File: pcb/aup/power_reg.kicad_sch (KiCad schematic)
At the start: 47 parts, among them Q2 AO3400A, Q3 AO3401A, U14 ISL80103IRAJZ-TK, U5 TPS563257DRLR, U6 ISL80103IRAJZ-TK, U8 TPS563257DRLR, U9 TPS563257DRLR

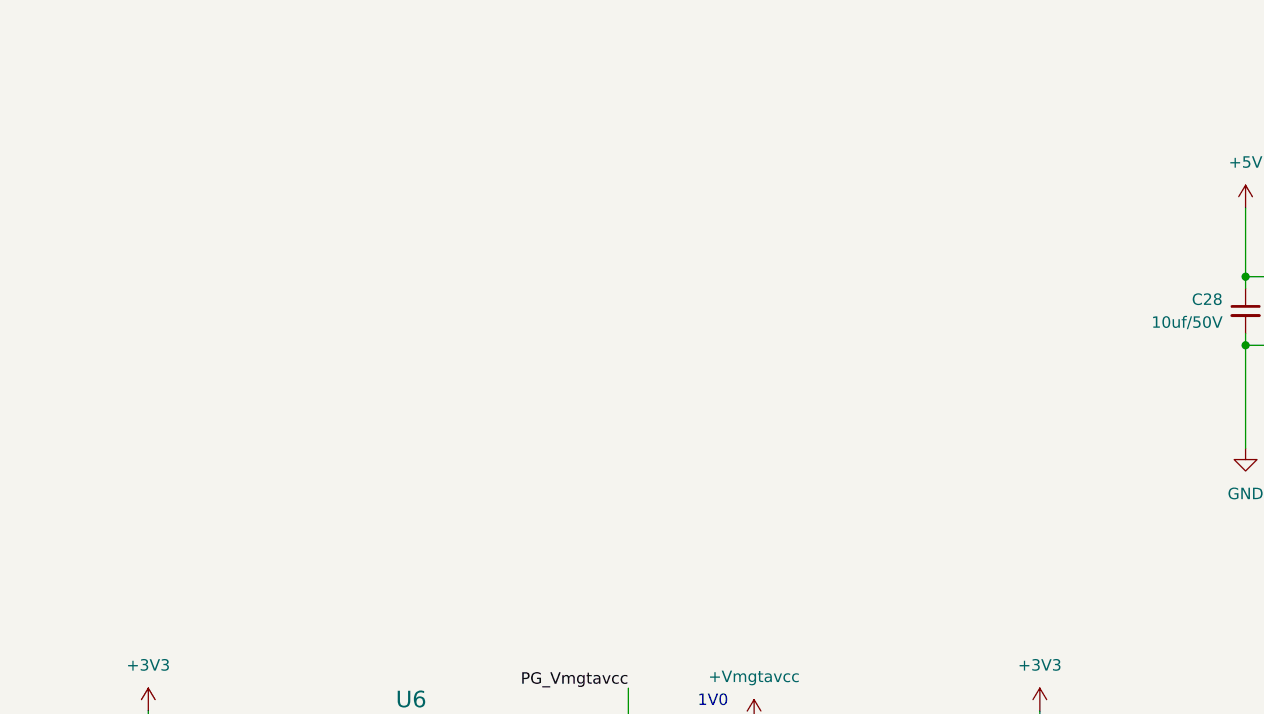
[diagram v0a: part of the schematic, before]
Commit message: Recovered 1v35
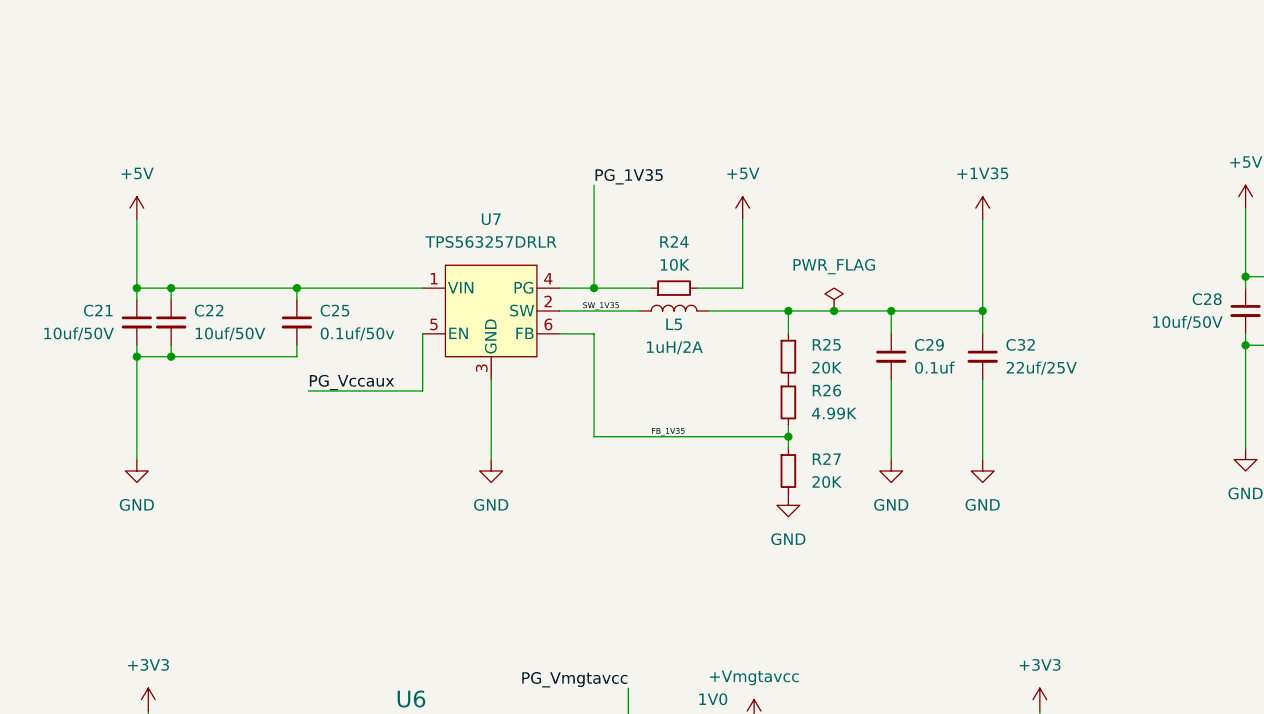
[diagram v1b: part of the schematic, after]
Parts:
- added C21, C22: 10uf/50V, Capacitor_SMD:C_0805_2012Metric, symbol !Misc:C_10uf_0805
- added C25: 0.1uf/50v, Capacitor_SMD:C_0603_1608Metric, symbol !Misc:C_0.1uf_0603
- added C29: 0.1uf, Capacitor_SMD:C_0402_1005Metric, symbol !Misc:C_0.1uf_0402
- added C32: 22uf/25V, Capacitor_SMD:C_0805_2012Metric, symbol !Misc:C_22uf_0805
- added L5: 1uH/2A, Inductor_SMD:L_1008_2520Metric, symbol !Misc:L_1uh_3A
- added R24: 10K, Resistor_SMD:R_0603_1608Metric, symbol !Misc:R_10K_0603
- added R25, R27: 20K, Resistor_SMD:R_0603_1608Metric, symbol !Misc:R_20K_0603
- added R26: 4.99K, Resistor_SMD:R_0603_1608Metric, symbol !Misc:R_4.99K_0603
- added U7: TPS563257DRLR, !Misc:SOT6_DRL_TEX, symbol !Misc:TPS563257DRLR
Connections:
- net +5V: now also C21.1, C22.1, C25.1, R24.2, U7.1 (VIN)
- net GND: now also C21.2, C22.2, C25.2, C29.2, C32.2, R27.2, U7.3 (GND)
- net PG_Vccaux: now also U7.5 (EN)
- new net: R25.2, R26.1
- new net +1V35: C29.1, C32.1, L5.2, R25.1
- new net FB_1V35: R26.2, R27.1, U7.6 (FB)
- new net PG_1V35: R24.1, U7.4 (PG)
- new net SW_1V35: L5.1, U7.2 (SW)

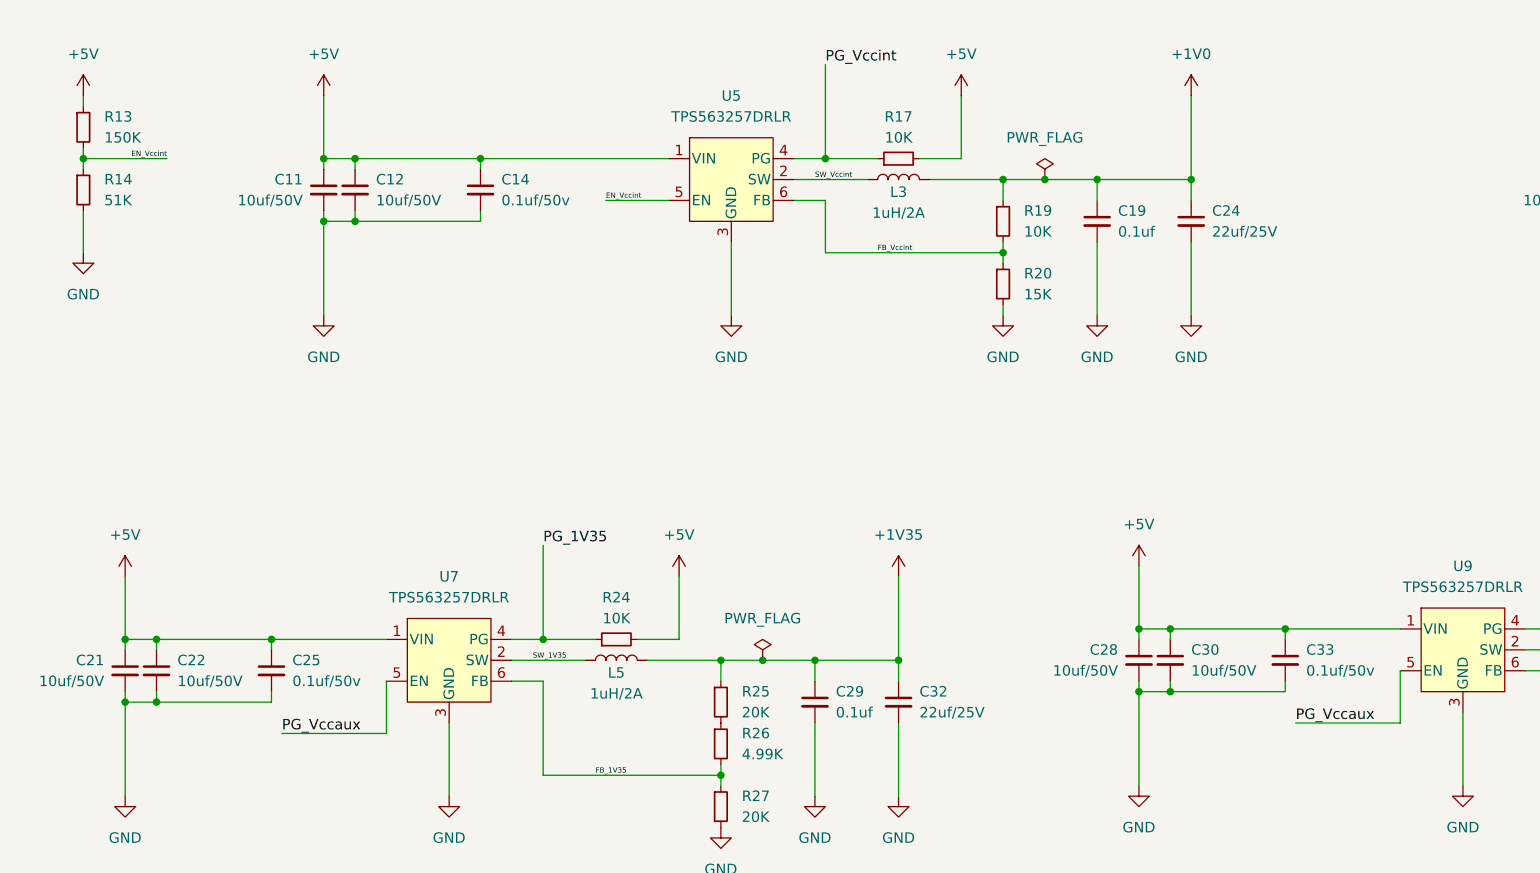
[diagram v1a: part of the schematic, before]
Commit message: Cleanup power layout
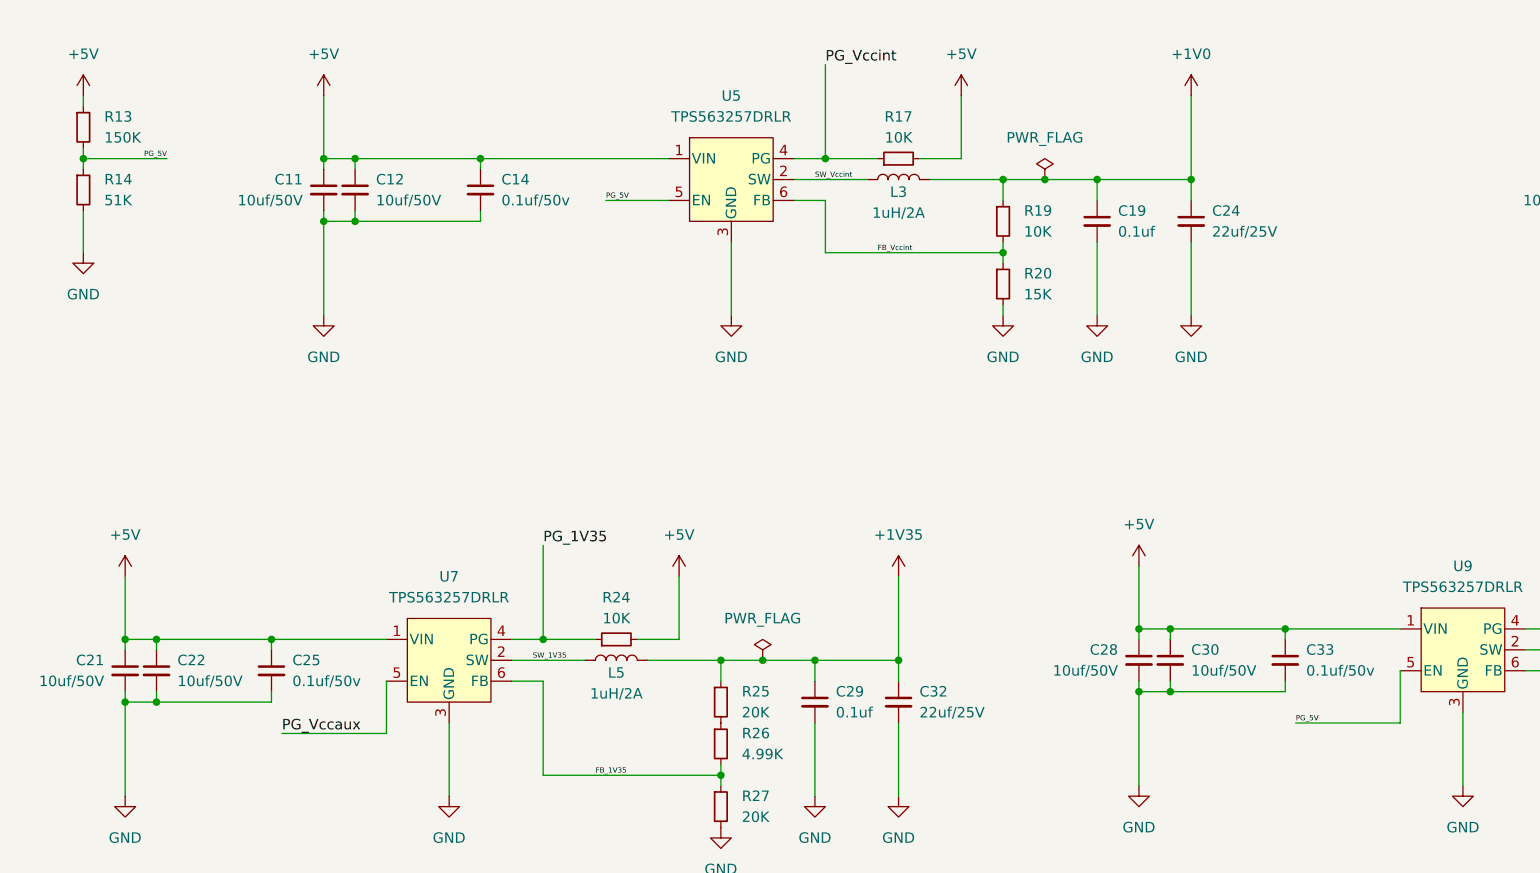
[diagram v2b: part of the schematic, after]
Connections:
- net PG_Vccaux: no longer U9.5 (EN)
- net EN_Vccint renamed PG_5V
- net PG_5V: now also U9.5 (EN)
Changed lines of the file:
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@@
 		)
 	)
-	(label "EN_Vccint"
+	(label "PG_5V"
 		(at 86.36 49.53 0)
 		(effects
@@
 		)
 	)
-	(label "EN_Vccint"
+	(label "PG_5V"
 		(at 33.02 44.45 180)
 		(effects
@@
 		)
 	)
-	(label "PG_Vccaux"
+	(label "PG_5V"
 		(at 170.18 113.03 0)
 		(effects
 			(font
-				(size 1.27 1.27)
-			)
-			(justify left bottom)
-		)
-	)
-	(rule_area
-		(polyline
-			(pts
-				(xy 114.3 141.732) (xy 114.3 196.088) (xy 213.36 196.215) (xy 213.36 141.605)
-			)
-			(stroke
-				(width 0)
-				(type dash)
-			)
-			(fill
-				(type none)
-			)
-		)
-	)
-	(rule_area
-		(polyline
-			(pts
-				(xy 194.31 22.86) (xy 194.31 76.454) (xy 328.041 77.216) (xy 328.295 23.368)
-			)
-			(stroke
-				(width 0)
-				(type dash)
-			)
-			(fill
-				(type none)
-			)
-		)
-	)
-	(rule_area
-		(polyline
-			(pts
-				(xy 15.24 141.732) (xy 15.24 196.088) (xy 109.22 196.215) (xy 109.22 141.605)
-			)
-			(stroke
-				(width 0)
-				(type dash)
-			)
-			(fill
-				(type none)
-			)
-		)
-	)
-	(rule_area
-		(polyline
-			(pts
-				(xy 138.43 82.55) (xy 138.3665 131.826) (xy 257.8735 132.334) (xy 257.81 82.55)
-			)
-			(stroke
-				(width 0)
-				(type dash)
-			)
-			(fill
-				(type none)
-			)
-		)
-	)
-	(rule_area
-		(polyline
-			(pts
-				(xy 39.37 22.86) (xy 39.37 76.454) (xy 170.307 76.454) (xy 170.561 22.606)
-			)
-			(stroke
-				(width 0)
-				(type dash)
-			)
-			(fill
-				(type none)
-			)
-		)
-	)
-	(rule_area
-		(polyline
-			(pts
-				(xy 15.24 82.55) (xy 15.1765 131.826) (xy 134.6835 132.334) (xy 134.62 82.55)
-			)
-			(stroke
+				(size 0.635 0.635)
+			)
+			(justify left bottom)
+		)
+	)
+	(rule_area
+		(polyline
+			(pts
+				(xy 114.3 141.732) (xy 114.3 196.088) (xy 213.36 196.088) (xy 213.36 141.605)
+			)
+			(stroke
+				(width 0)
+				(type dash)
+			)
+			(fill
+				(type none)
+			)
+		)
+	)
+	(rule_area
+		(polyline
+			(pts
+				(xy 15.24 82.55) (xy 15.24 132.842) (xy 134.874 132.842) (xy 134.62 82.55)
+			)
+			(stroke
+				(width 0)
+				(type dash)
+			)
+			(fill
+				(type none)
+			)
+		)
+	)
+	(rule_area
+		(polyline
+			(pts
+				(xy 138.43 82.55) (xy 138.43 132.842) (xy 257.81 132.842) (xy 257.81 82.55)
+			)
+			(stroke
+				(width 0)
+				(type dash)
+			)
+			(fill
+				(type none)
+			)
+		)
+	)
+	(rule_area
+		(polyline
+			(pts
+				(xy 39.116 22.86) (xy 39.116 76.2) (xy 169.926 76.2) (xy 169.926 22.86)
+			)
+			(stroke
+				(width 0)
+				(type dash)
+			)
+			(fill
+				(type none)
+			)
+		)
+	)
+	(rule_area
+		(polyline
+			(pts
+				(xy 194.31 22.86) (xy 194.31 75.946) (xy 327.914 75.946) (xy 327.914 22.86)
+			)
+			(stroke
+				(width 0)
+				(type dash)
+			)
+			(fill
+				(type none)
+			)
+		)
+	)
+	(rule_area
+		(polyline
+			(pts
+				(xy 15.24 141.732) (xy 15.24 196.088) (xy 109.22 196.088) (xy 109.22 141.605)
+			)
+			(stroke
